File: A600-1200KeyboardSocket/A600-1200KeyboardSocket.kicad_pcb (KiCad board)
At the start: 2 copper layers, 21.6 x 26.7 mm, 2 parts, among them J1 KBD, U1 68HC711_PLCC

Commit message: A600-1200KeyboardSocket : better symbol for PLCC socket
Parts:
- removed U1: 68HC711_PLCC, Package_LCC:PLCC-44_THT-Socket
- added J2: PLCC-44_Socket-on-top, Package_LCC:PLCC-44_THT-Socket, B.Cu at (144.8, 96.5)

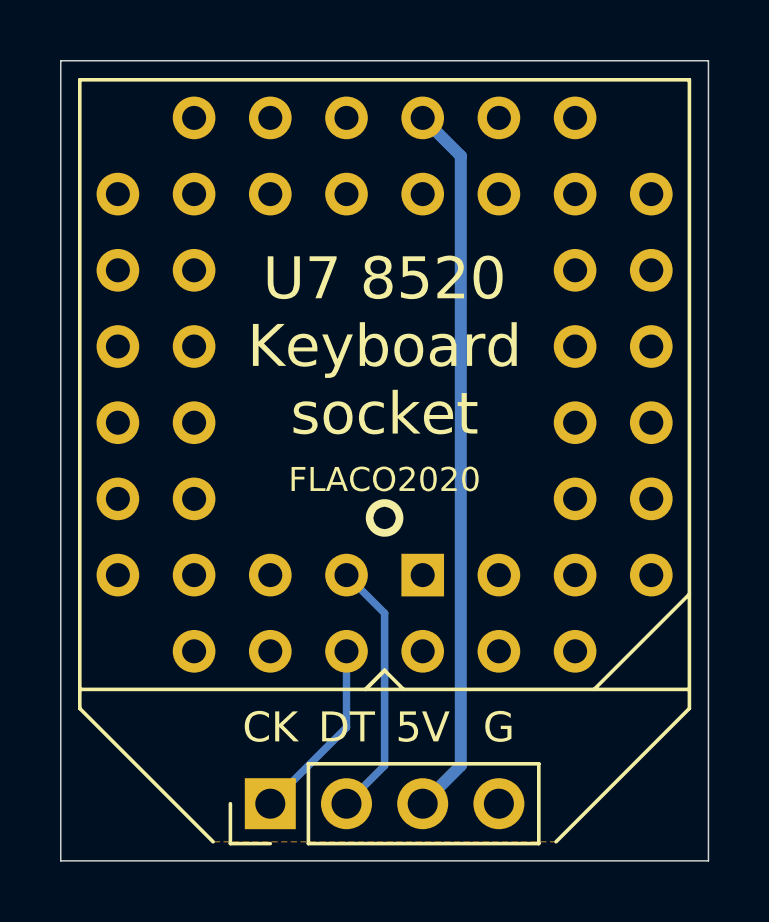
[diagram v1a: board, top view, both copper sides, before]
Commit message: A1200PcmciaResetFix, A600-1200KeyboardSocket : update socket symbol and footprint, no PCB change
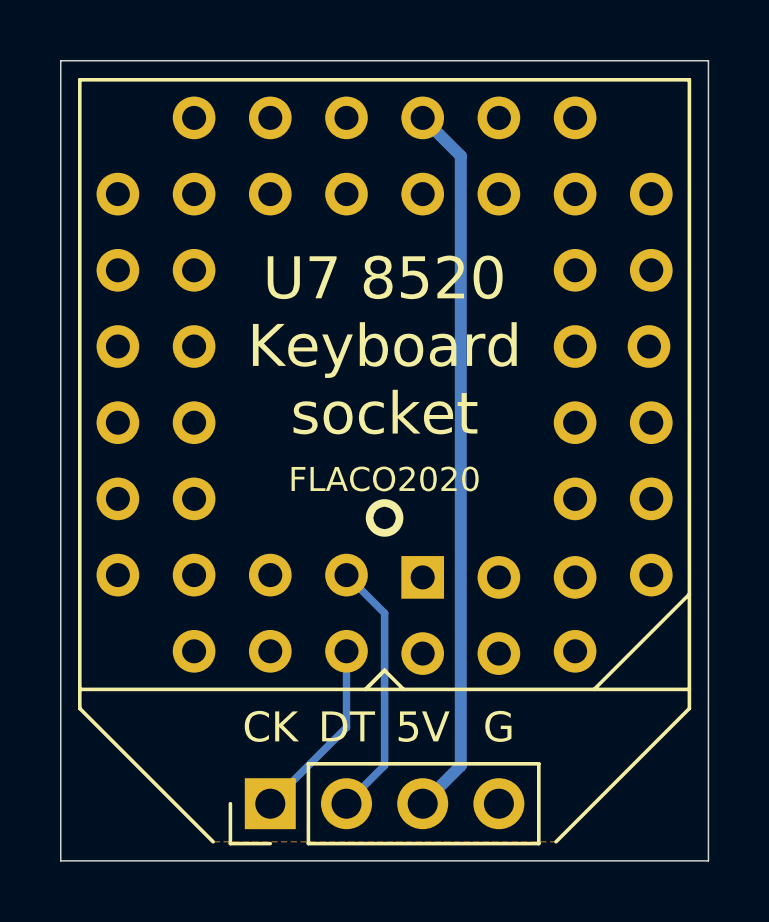
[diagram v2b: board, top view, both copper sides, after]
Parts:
- J2: footprint Package_LCC:PLCC-44_THT-Socket -> Sassa:PLCC-44_THT-SocketOnTop
- moved J2 9.16 mm to (149.9, 88.9), turned to 90 degrees
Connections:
- J2 pad 2: /KB_CLOCK -> unconnected-(J2-Pad2)
- J2 pad 22: unconnected-(J2-Pad22) -> +5V
- J2 pad 24: +5V -> unconnected-(J2-Pad24)
- J2 pad 3: /KB_DATA -> unconnected-(J2-Pad3)
- J2 pad 43: unconnected-(J2-Pad43) -> /KB_DATA
- J2 pad 44: unconnected-(J2-Pad44) -> /KB_CLOCK
